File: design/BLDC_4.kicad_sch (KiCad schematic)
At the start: 27 parts, among them J1 BM10B-GHS-TBT_LF__SN__N_, K1 SERVO, P1 CANBUS, P2 HALL/Encoder, P3 PWR_COMM, P4 IN+, P5 IN-, P6 MOTOR3, P7 MOTOR2, P8 MOTOR1, X1 MINI-USB-SHIELD-32005-201

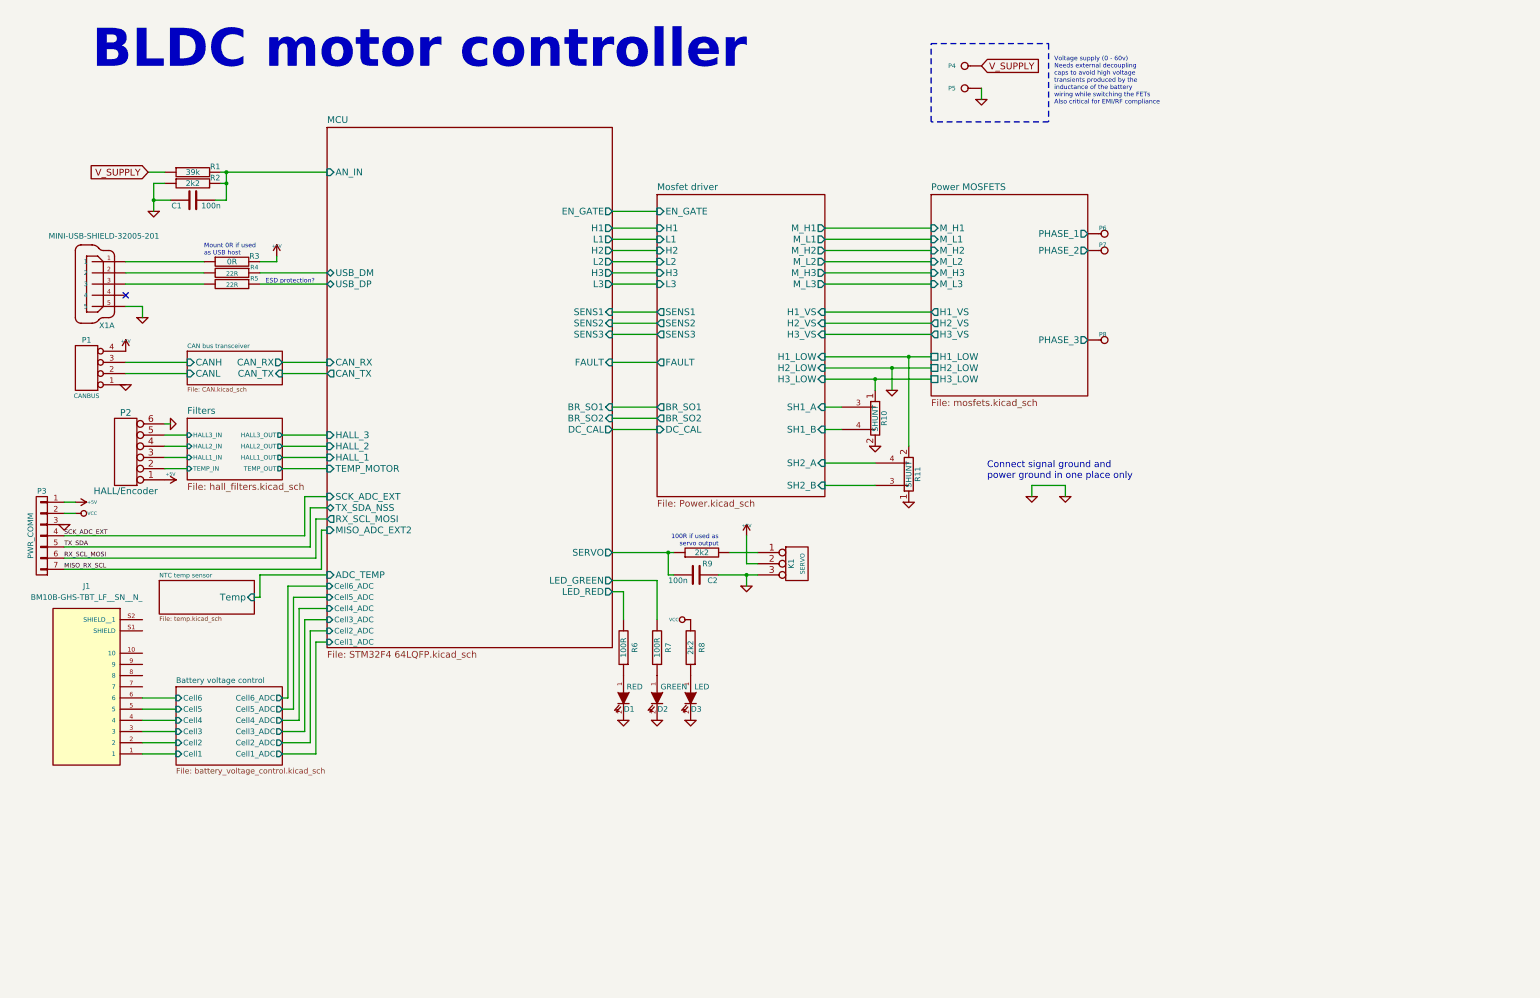
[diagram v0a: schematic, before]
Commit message: added battery balancer
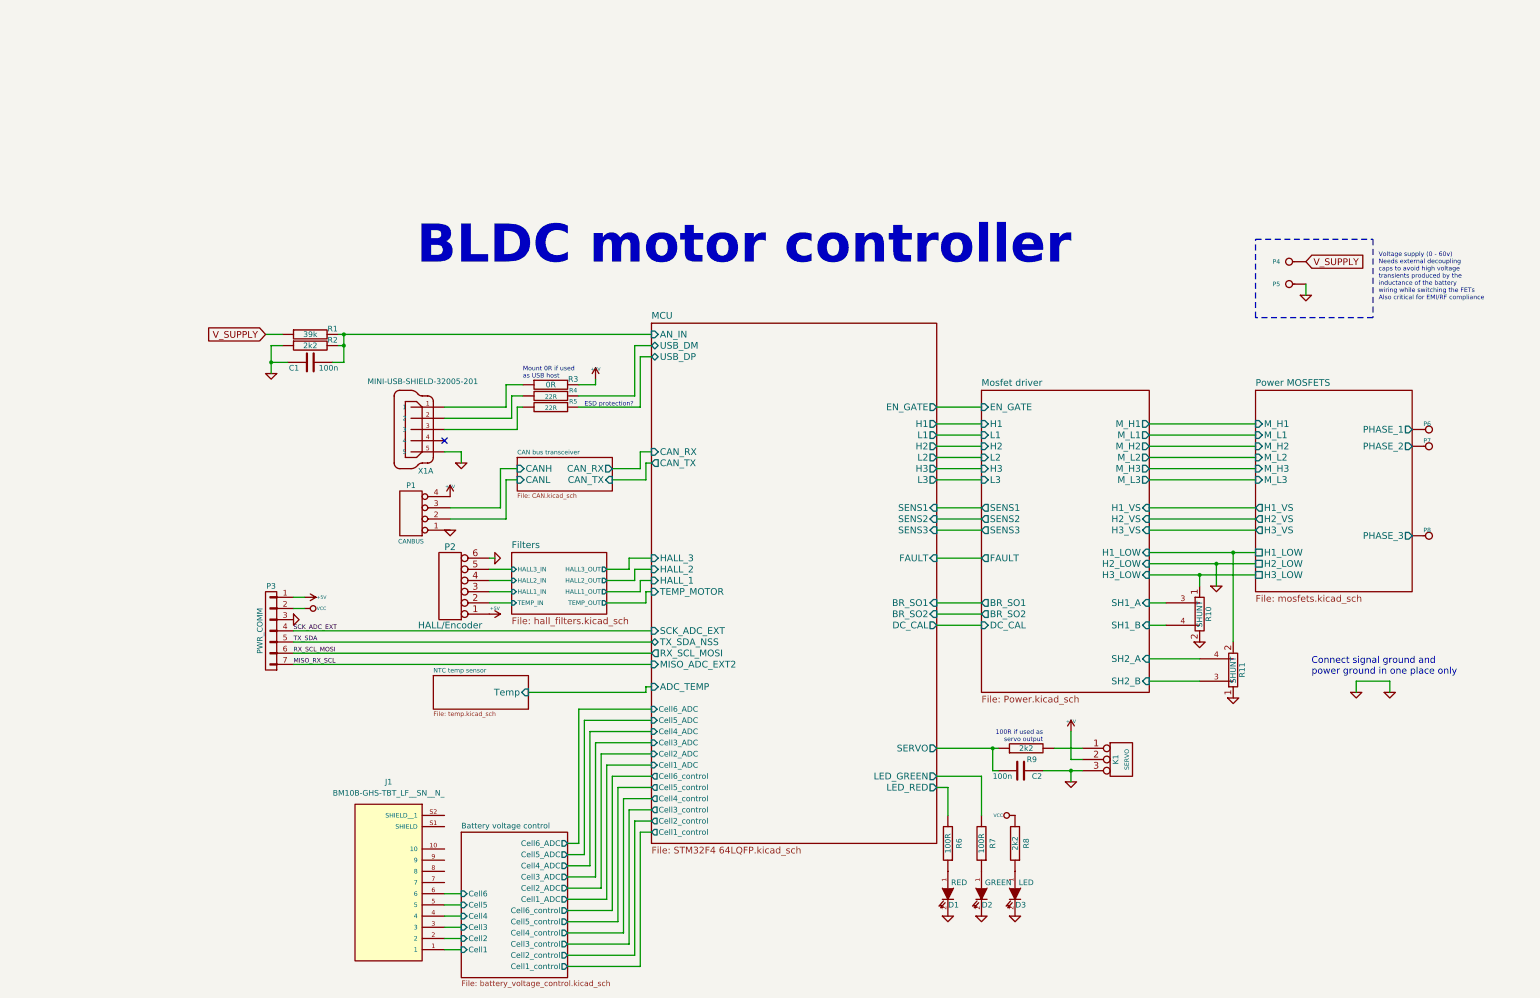
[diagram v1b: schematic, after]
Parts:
- J1: footprint BM10B-GHS-TBT_LF__SN__N_:JST_BM10B-GHS-TBT_LF__SN__N_ -> jst-gh:JST_BM10B-GHS-TBT_LF__SN__N_
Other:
- sheet Battery voltage control ports: added Cell1_control, Cell2_control, Cell3_control, Cell4_control, Cell5_control, Cell6_control; removed none
- sheet MCU ports: added Cell1_control, Cell2_control, Cell3_control, Cell4_control, Cell5_control, Cell6_control; removed none
- moved on the sheet: C1, C2, D1, D2, D3, J1, K1, P1, P2, P3, P4, P5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

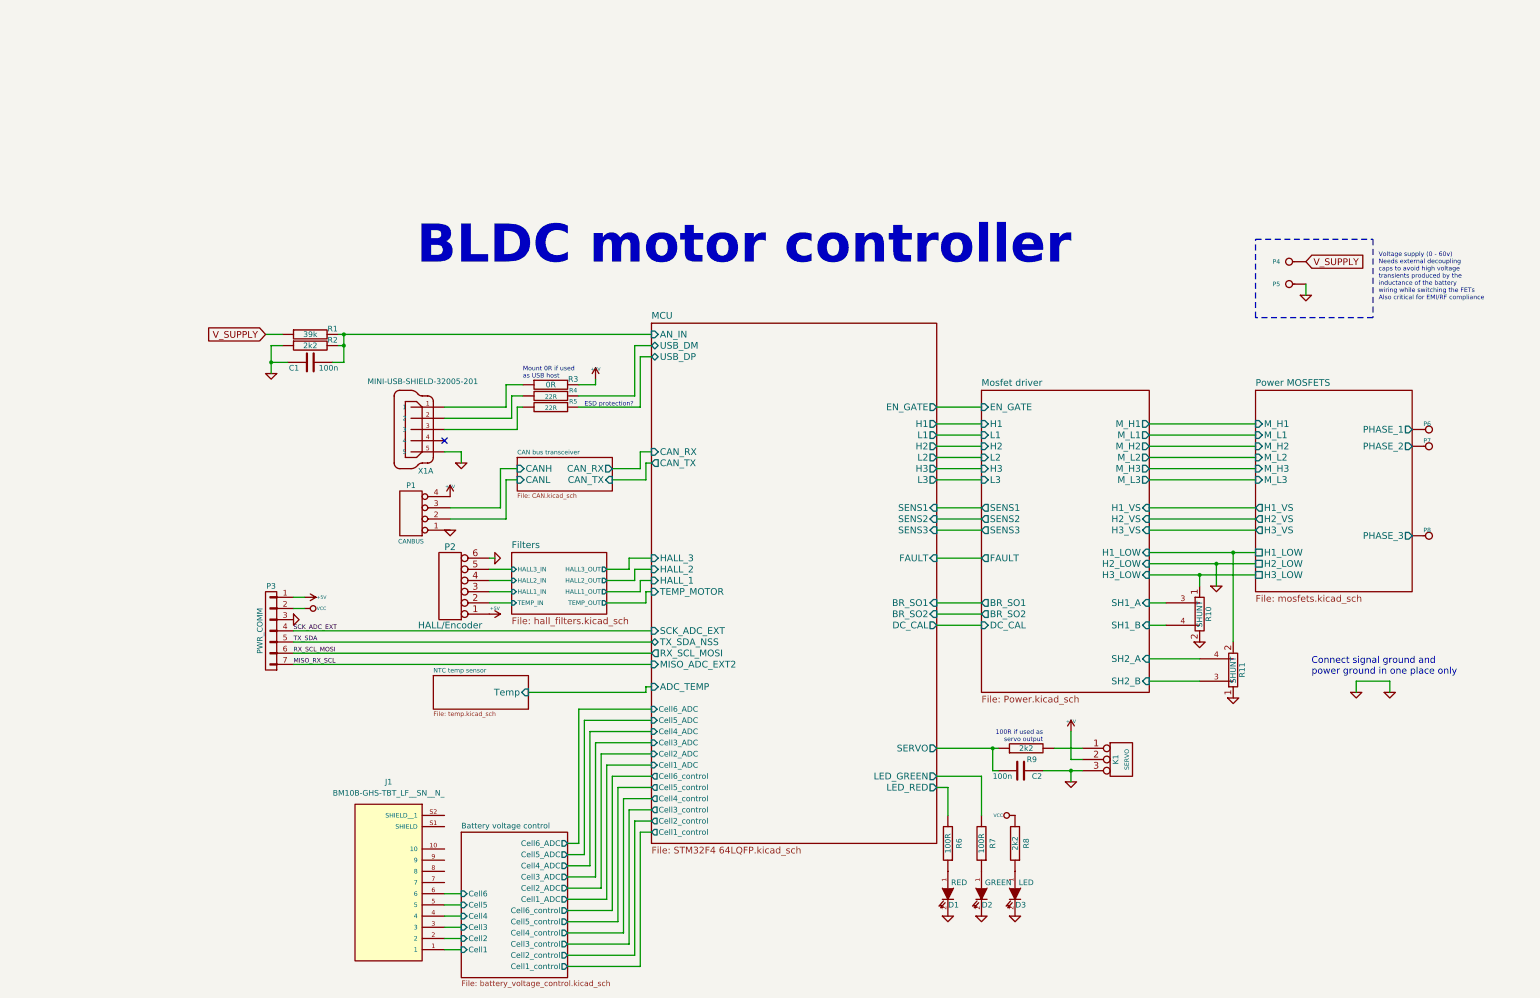
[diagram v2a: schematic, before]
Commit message: added usb connector
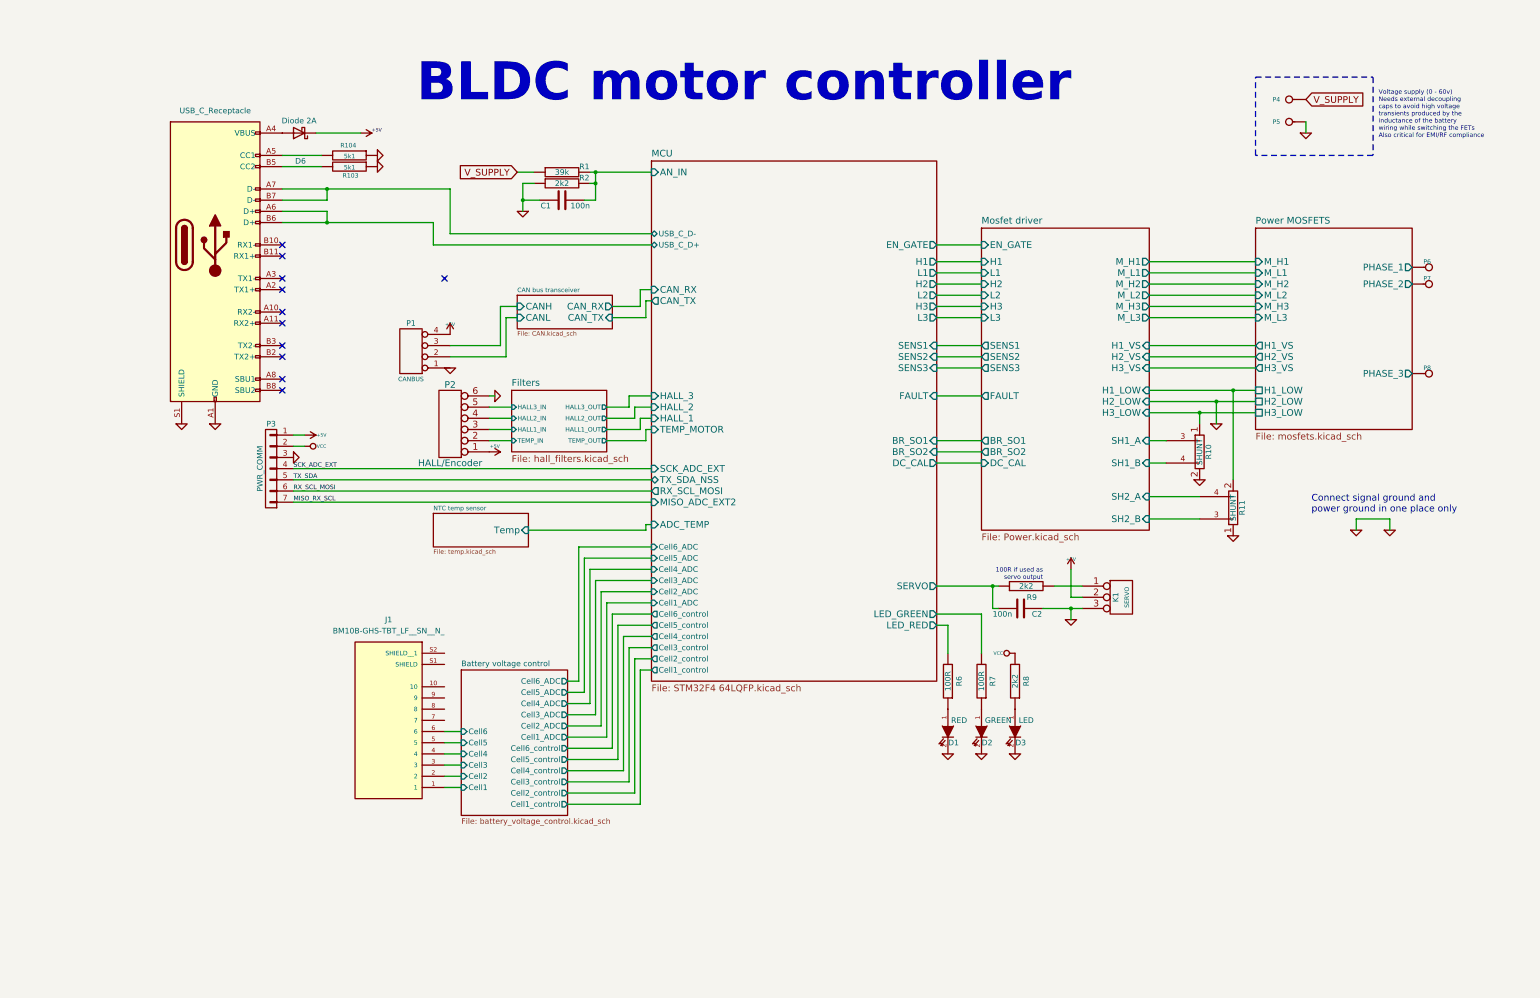
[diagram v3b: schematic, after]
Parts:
- removed R3: 0R, CRF1:SMD-0603_r, symbol BLDC_4-rescue:R-RESCUE-BLDC_4
- removed X1: MINI-USB-SHIELD-32005-201, CRF1:USB-UX60R-MB-5ST, symbol BLDC_4-rescue:MINI-USB-SCHIELD-32005-201
- added D6: Diode 2A, Diode_SMD:D_SOD-323F, symbol Diode:PMEG1020EJ
- added J2: USB_C_Receptacle, symbol Connector:USB_C_Receptacle
- R103: renamed from R4; value 22R -> 5k1
- R104: renamed from R5; value 22R -> 5k1
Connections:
- net MCU/USB_DM is gone; now on net GND: R103.1
- net MCU/USB_DP is gone; now on net GND: R104.1
- net +5V: now also D6.1 (K)
- net GND: now also J2.A1 (GND), J2.A12 (GND), J2.B1 (GND), J2.B12 (GND), J2.S1 (SHIELD)
- net at R103.2: now also J2.B5 (CC2)
- net at R104.2: now also J2.A5 (CC1)
- new net: D6.2 (A), J2.A4 (VBUS), J2.A9 (VBUS), J2.B4 (VBUS), J2.B9 (VBUS)
- new net MCU/USB_C_D+: J2.A6 (D+), J2.B6 (D+)
- new net MCU/USB_C_D-: J2.A7 (D-), J2.B7 (D-)
- no-connect marks 1 -> 11
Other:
- sheet MCU ports: added USB_C_D+, USB_C_D-; removed USB_DM, USB_DP
- note removed: "ESD protection?"
- note removed: "Mount 0R if used as USB host"
- moved on the sheet: C1, C2, D1, D2, D3, J1, K1, P1, P2, P3, P4, P5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

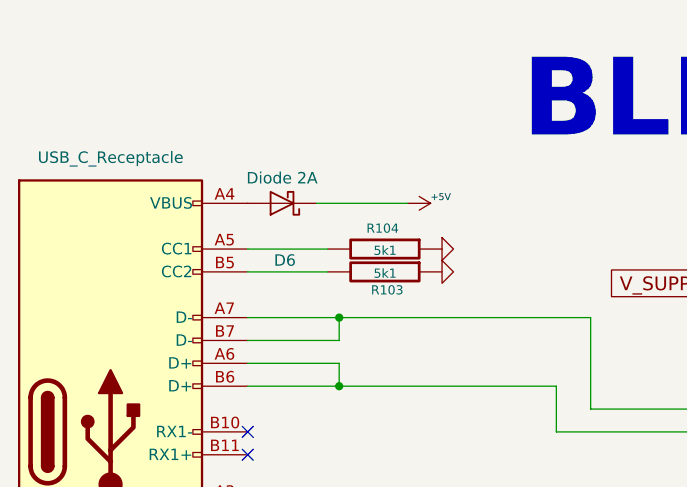
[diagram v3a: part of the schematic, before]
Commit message: change diod with usb connector
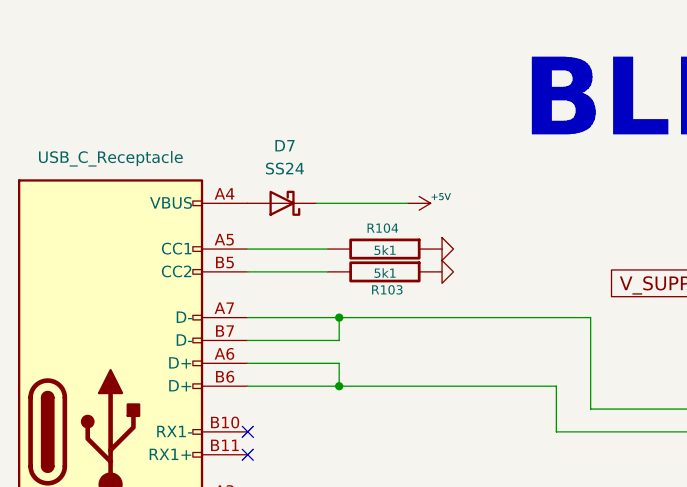
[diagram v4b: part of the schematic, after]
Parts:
- removed D6: Diode 2A, Diode_SMD:D_SOD-323F, symbol Diode:PMEG1020EJ
- added D7: SS24, Diode_SMD:D_SMA, symbol Diode:SS24
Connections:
- net +5V: now also D7.1 (K)
- net at J2.A4 (VBUS), J2.A9 (VBUS), J2.B4 (VBUS)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: now also D7.2 (A)
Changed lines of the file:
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@@
 			"tIpRNXDlW8jnedCpIRPSpBQMPKZf1nr419dPrpEJIURQ0aGXA5jAqYvkkY/Hn5EnaVIdSeSSsC0/"
 			"rswYMAEIRO8a/Qjx5LBeNj4LWPHXLrDiMb0GSPMAWq4nAOqPHxVuDuhV+4MAFH/tAige02t/6PSS"
-			"A1qUZaohHanuKsaJE9YHIyrIHN5e4xLj/MEshdRgOElffg=="
+			"A1qUZaohHanuKsaJE9YHIyrIHN5e4xLj/MEshdRgOElffgAAAAAAAAAAAAAAAAAAAAAAAAAAAAAA"
+			"AAAAAAAAAAAAAAAAAAAAAAAAAAAAAAAAAAAAAAAAAAAAAAAAAAAAAAAAAAAAAAAAAAAAAAAAAAAA"
+			"AAAAAAAAAAAAAAAAAAAAAAAAAAAAAAAAAAAAAAAAAAAAAAAAAAAAAAAAAAAAAAAAAAAAAAAAAAAA"
+			"AAAAAAAAAAAAAAAAAAAAAAAAAAAAAAAAAAAAAAAAAAAAAAAAAAAAAAAAAAAAAAAAAAAAAAAAAAAA"
+			"AAAAAAAAAAAAAAAAAAAAAAAAAAAAAAAAAAAAAAAAAAAAAAAAAAAAAAAAAAAAAAAAAAAAAAAAAAAA"
+			"AAAAAAAAAAAAAAAAAAAAAAAAAAAAAAAAAAAAAAAAAAAAAAAAAAAAAAAAAAAAAAAAAAAAAAAAAAAA"
+			"AAAAAAAAAAAAAAAAAAAAAAAAAAAAAAAAAAAAAAAAAAAAAAAAAAAAAAAAAAAAAAAAAAAAAAAAAAAA"
+			"AAAAAAAAAAAAAAAAAAAAAAAAAAAAAAAAAAAAAAAAAAAAAAAAAAAAAAAAAAAAAAAAAAAAAAAAAAAA"
+			"AAAAAAAAAAAAAAAAAAAAAAAAAAAAAAAAAAAAAAAAAAAAAAAAAAAAAAAAAAAAAAAAAAAAAAAAAAAA"
+			"AAAAAAAAAAAAAAAAAAAAAAAAAAAAAAAAAAAAAAAAAAAAAAAAAAAAAAAAAAAAAAAAAAAAAAAAAAAA"
+			"AAAAAAAAAAAAAAAAAAAAAAAAAAAAAAAAAAAAAAAAAAAAAAAAAAAAAAAAAAAAAAAAAAAAAAAAAAAA"
+			"AAAAAAAAAAAAAAAAAAAAAAAAAAAAAAAAAAAAAAAAAAAAAAAAAAAAAAAAAAAAAAAAAAAAAAAAAAAA"
+			"AAAAAAAAAAAAAAAAAAAAAAAAAAAAAAAAAAAAAAAAAAAAAAAAAAAAAAAAAAAAAAAAAAAAAAAAAAAA"
+			"AAAAAAAAAAAAAAAAAAAAAAAAAAAAAAAAAAAAAAAAAAAAAAAAAAAAAAAAAAAAAAAAAAAAAAAAAAAA"
+			"AAAAAAAAAAAAAAAAAAAAAAAAAAAAAAAAAAAAAAAAAAAAAAAAAAAAAAAAAAAAAAAAAAAAAAAAAAAA"
+			"AAAAAAAAAAAAAAAAAAAAAAAAAAAAAAAAAAAAAAAAAAAAAAAAAAAAAAAAAAAAAAAAAAAAAAAAAAAA"
+			"AAAAAAAAAAAAAAAAAAAAAAAAAAAAAAAAAAAAAAAAAAAAAAAAAAAAAAAAAAAAAAAAAAAAAAAAAAAA"
+			"AAAAAAAAAAAAAAAAAAAAAAAAAAAAAAAAAAAAAAAAAAAAAAAAAAAAAAAAAAAAAAAAAAAAAAAAAAAA"
+			"AAAAAAAAAAAAAAAAAAAAAAAAAAAAAAAAAAAAAAAAAAAAAA=="
 		)
 	)
@@
 			"bABzAEQAUAAyADYAbABQAEEAMABNADkAWAByAHIAMwBFAEEAeQB1AEQAKwAwAFEAMABiAE4AcgBS"
 			"ADEAOQAxAEwAaAA3AGUAMgAzADMAeQA0AHYATAA5AGYAMgBqAFgAagA5ADkAYgBQAFAAUABsAHMA"
-			"eg=="
+			"egBjAC8AbgB5ADUAYwBPAEcARABhAE4AKwB6AEMAMABIAHQAOQBHAFoATABTADAAdAA0ADgAYQBO"
+			"AG8AMABzAGUAKwAyAEkARABuAFIAawBLAGgAUgBpAFEAZgBmAFYAaAB2AEEAbQA5AEoARQBsADAA"
+			"OQBYAEEANAAvAFAAbQA3AC8ANgBZAHoAWABTADUAaAA4AE8ARABCAGwATgBKAFcAcgBGAGgAQgBa"
+			"AHoAYgBDAGkAVwAzAGIAdABtAG4ARwB2AHgARgBPAGIATgB5ADQAVQBUAE4AegArAFoAZAB2AEwA"
+			"VgArAHUATgBVAGoATQArAC8ASgB2AFQAbAAwAHIAVQAyAEMAQwBTADIAYQBVAEUAeQBVAEsAYwBI"
+			"AHoAaQAxAE0ANwBnAHEATgAvADIAdQB1ADkAVQBkAE8ANwBSAFEAeABTAHAANgA1AE8AWABSAE8A"
+			"ZABnAGoARwBuADUAQwBUAFAASQArAC8AegB6AGUAaQA2AFIAUAA0ADYARgA2AGgAcwBhAEwASwB4"
+			"ADQAUABDAFUAQQBRAFkAUAAxADAANQBQAGUAcQAvAHYAWgBqAGoAMgAwAGkAawBwAFYAVgBaAFgA"
+			"bQBEAEUAegA0AHMAZQBjAG4AcgBxAFcAOABjAFQAbwBoAGkAbQBMAEgAagBoADAAcAA1AE4ASAA0"
+			"AGIAagA1AG0AZQA4AGQAZQAvAE4AbgBCAEYANQBJADYAbAAxAGoAWQBIAEsATwAwADAAUgBmAGQA"
+			"eQBvAHEAVgAyAEsARQBmAHQAZQAxAGUAbQAvAHYAWQBlAGcAQQBuAFQANQA1AFMAbwByAEkAbgA0"
+			"AEEARwBJAHMANQB5AEEANABlADkAWABiAEIAcwB3AEEARgAwADIAYgA2AGgAYQB4ADkASABnAHQA"
+			"NgBrAFoAVABMACsASwAvAHAAVAB6AGcATAB1ADUAZwB2AHAAWgBXAFYAagB2ACsARgBkAEIARQBI"
+			"AEoAcgB5AFcATgBtAHYASQBRAEoAdABrAFcAMgB5AHcAZABaAFcALwBMAFkAQgBLAE4AMgBRAGsA"
+			"ZwBrAEUAaQBrAHIASwA3AFAAYwBhAHEAWgBVADAASwBYAHkAYwBxAHUAYwBGAFUAUABtAHoASABq"
+			"AGEAYgBJAHkARQBtADYATABOAFEAdwB5AHIAbwAxAEgAUgB5AC8AUwBSAEkAMABmAEcAagBCAG4A"
+			"RAArAHoARQBCADQATwBUAEoAawA4AHgAcwBkAHYAQwBUAHcAMwBSAG0ASgBCAEkAWgBNAG0AUQBJ"
+			"AG4AYgBsAHoAWABUAHcARgBVAGgAVABGAG8AVQBPAEgAaABrAEsAaAAxAHQAWgBXAEMAbgBtAE4A"
+			"WA=="
 		)
 	)
@@
 	)
 	(symbol
-		(lib_id "Diode:PMEG1020EJ")
+		(lib_id "Diode:SS24")
 		(at 76.2 45.72 180)
 		(unit 1)
@@
 		(on_board yes)
 		(dnp no)
-		(property "Reference" "D6"
-			(at 76.5175 52.07 0)
+		(fields_autoplaced yes)
+		(property "Reference" "D7"
+			(at 76.5175 39.37 0)
 			(effects
 				(font
@@
 			)
 		)
-		(property "Value" "Diode 2A"
-			(at 76.2 42.926 0)
+		(property "Value" "SS24"
+			(at 76.5175 41.91 0)
 			(effects
 				(font
@@
 			)
 		)
-		(property "Footprint" "Diode_SMD:D_SOD-323F"
+		(property "Footprint" "Diode_SMD:D_SMA"
 			(at 76.2 41.275 0)
 			(effects
@@
 			)
 		)
-		(property "Datasheet" "https://assets.nexperia.com/documents/data-sheet/PMEG1020EH_EJ.pdf"
+		(property "Datasheet" "https://www.vishay.com/docs/88748/ss22.pdf"
 			(at 76.2 45.72 0)
 			(effects
@@
 			)
 		)
-		(property "Description" "10V, 2A ultra low Vf MEGA Schottky barrier rectifier, SOD-323F"
+		(property "Description" "40V 2A Schottky Diode, SMA"
 			(at 76.2 45.72 0)
 			(effects
@@
 			)
 		)
-		(pin "1"
-		)
 		(pin "2"
 		)
+		(pin "1"
+		)
 		(instances
-			(project "BLDC_4"
+			(project ""
 				(path "/4e37e2da-f0c5-4e16-8054-f3124781dd7a"
-					(reference "D6")
+					(reference "D7")
 					(unit 1)
 				)
